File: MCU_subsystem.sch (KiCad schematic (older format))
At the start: 14 parts

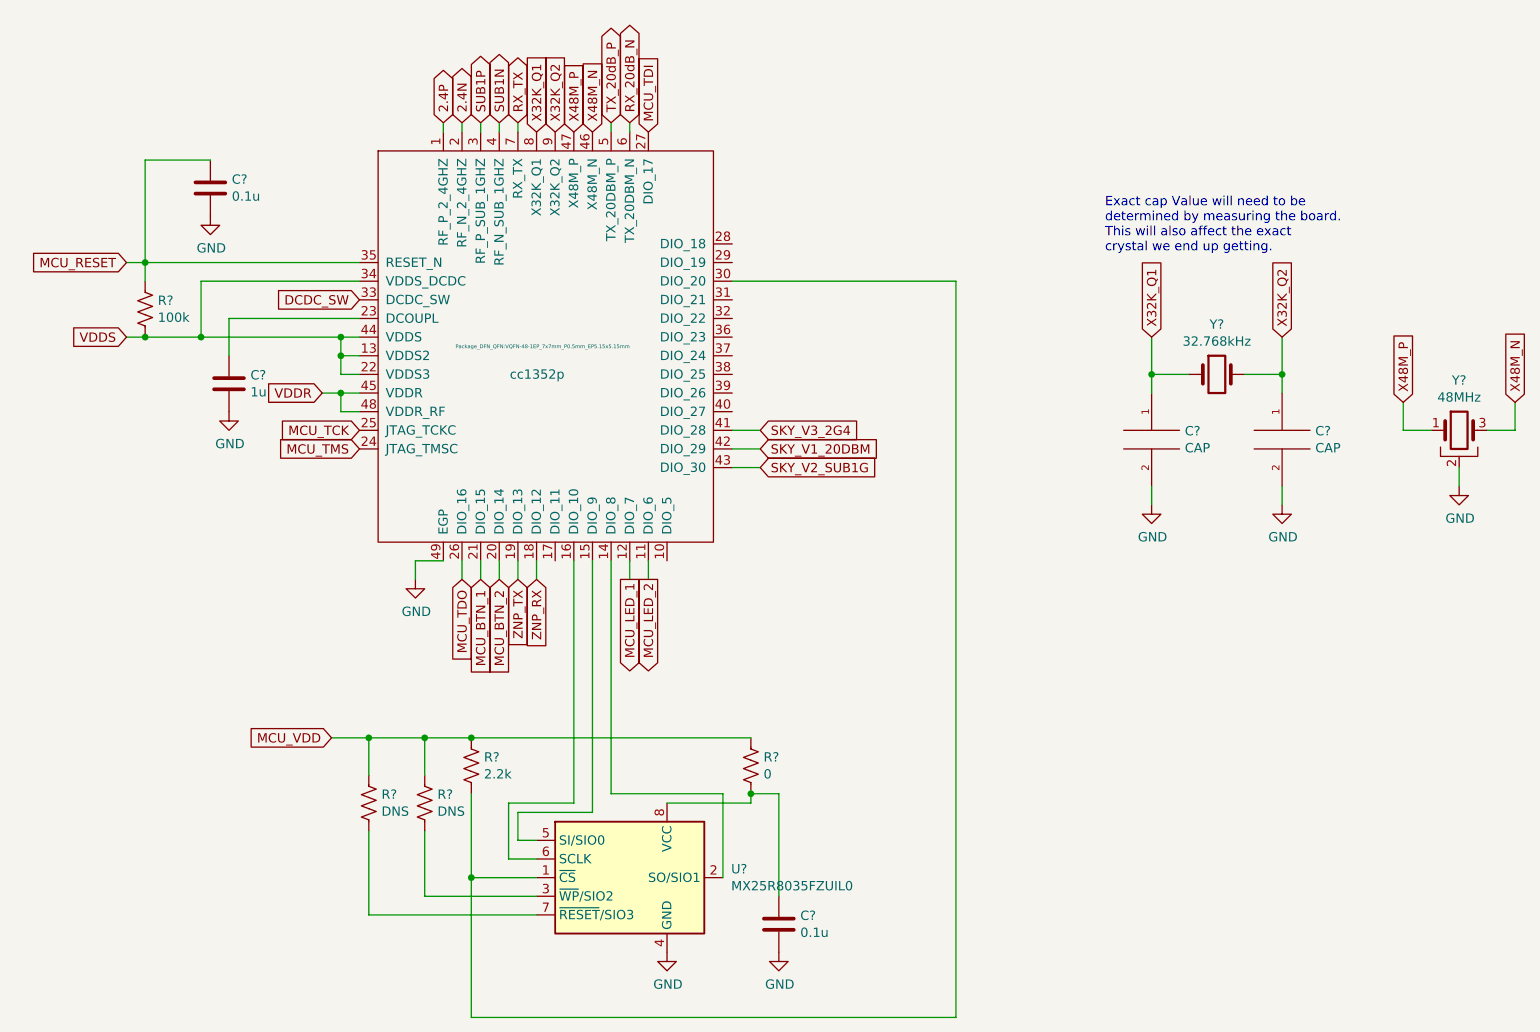
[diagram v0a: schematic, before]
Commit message: Revert "Added Flash IC and PB/LED footprints."
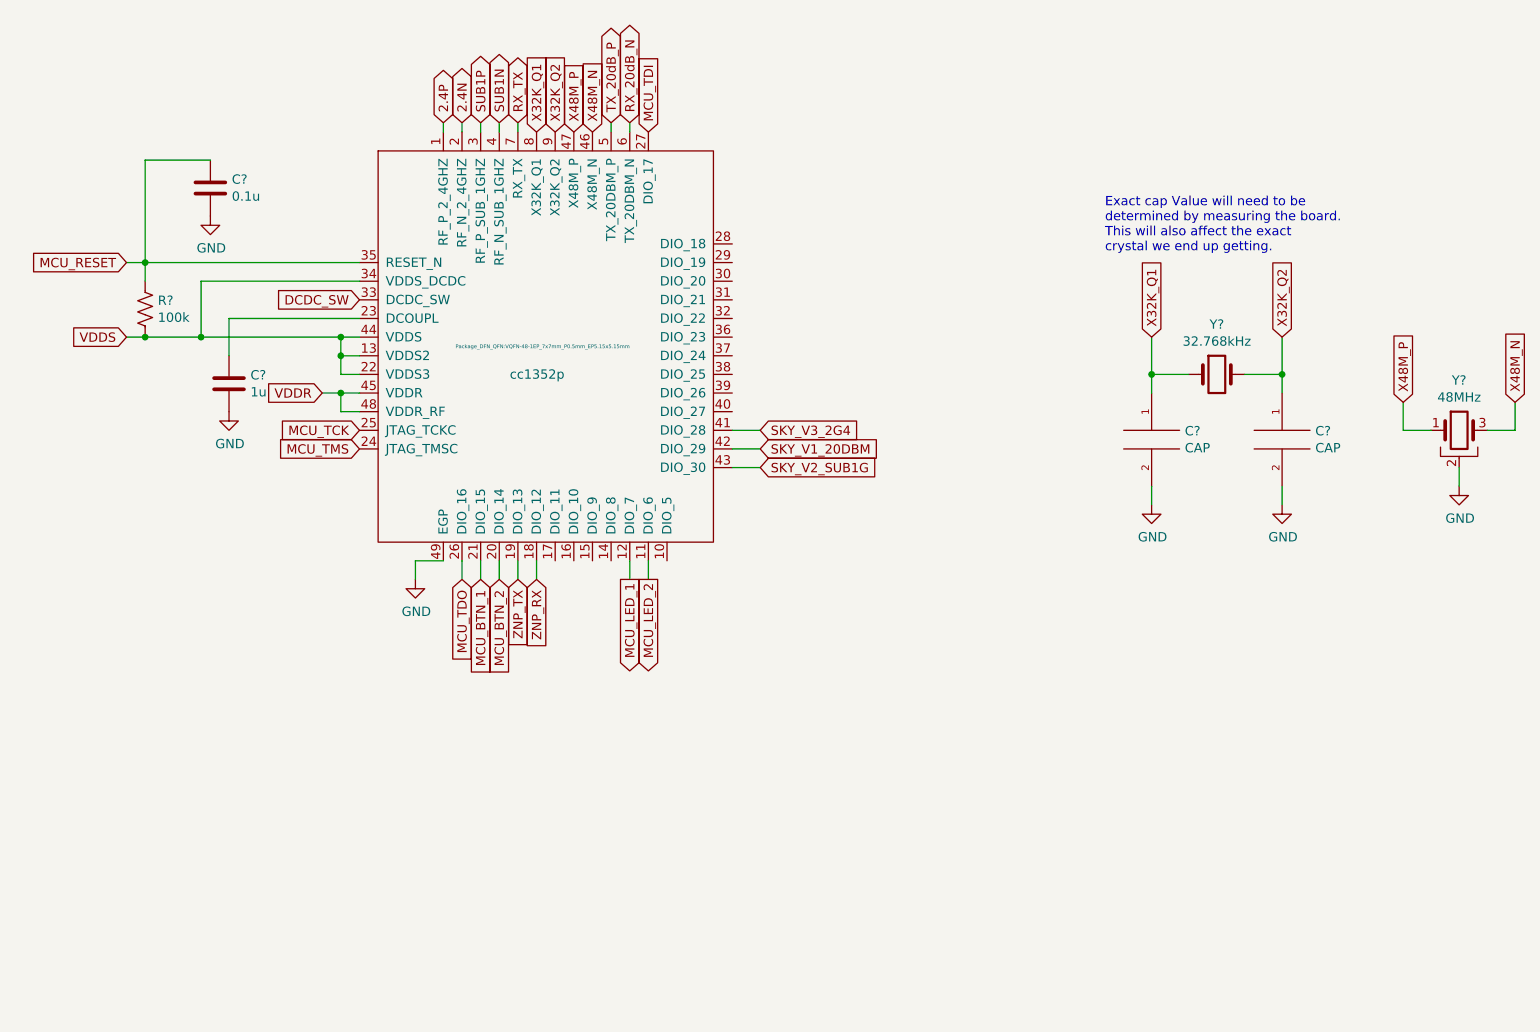
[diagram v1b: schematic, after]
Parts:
- removed C?: 0.1u, Capacitor_SMD:C_0805_2012Metric_Pad1.18x1.45mm_HandSolder, symbol Device:C
- removed R?: 2.2k, Resistor_SMD:R_0805_2012Metric_Pad1.20x1.40mm_HandSolder, symbol Device:R_US
- removed R?: 0, Resistor_SMD:R_0805_2012Metric_Pad1.20x1.40mm_HandSolder, symbol Device:R_US
- removed R? (x2): DNS, Resistor_SMD:R_0805_2012Metric_Pad1.20x1.40mm_HandSolder, symbol Device:R_US
- removed U?: MX25R8035FZUIL0, Package_SO:SOP-8_5.28x5.23mm_P1.27mm, symbol FLASH:MX25R8035FZUIL0
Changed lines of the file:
@@
 Text Notes 6850 3350 0    50   ~ 0
 Exact cap Value will need to be \ndetermined by measuring the board. \nThis will also affect the exact \ncrystal we end up getting.
-$Comp
-L power:GND #PWR?
-U 1 1 614D787A
-P 4500 7100
-F 0 "#PWR?" H 4500 6850 50  0001 C CNN
-F 1 "GND" H 4505 6927 50  0000 C CNN
-F 2 "" H 4500 7100 50  0001 C CNN
-F 3 "" H 4500 7100 50  0001 C CNN
-	1    4500 7100
-	1    0    0    -1
-$EndComp
-$Comp
-L power:GND #PWR?
-U 1 1 614D8142
-P 5100 7100
-F 0 "#PWR?" H 5100 6850 50  0001 C CNN
-F 1 "GND" H 5105 6927 50  0000 C CNN
-F 2 "" H 5100 7100 50  0001 C CNN
-F 3 "" H 5100 7100 50  0001 C CNN
-	1    5100 7100
-	1    0    0    -1
-$EndComp
-Text GLabel 2700 5950 0    50   Input ~ 0
-MCU_VDD
-$Comp
-L Device:R_US R?
-U 1 1 614D91BC
-P 3450 6100
-F 0 "R?" H 3518 6146 50  0000 L CNN
-F 1 "2.2k" H 3518 6055 50  0000 L CNN
-F 2 "Resistor_SMD:R_0805_2012Metric_Pad1.20x1.40mm_HandSolder" V 3490 6090 50  0001 C CNN
-F 3 "~" H 3450 6100 50  0001 C CNN
-	1    3450 6100
-	1    0    0    -1
-$EndComp
-Wire Wire Line
-	3800 6700 3450 6700
-Wire Wire Line
-	3450 6700 3450 6250
-Wire Wire Line
-	3200 5950 3450 5950
-$Comp
-L Device:R_US R?
-U 1 1 614DDC0C
-P 4950 6100
-F 0 "R?" H 5018 6146 50  0000 L CNN
-F 1 "0" H 5018 6055 50  0000 L CNN
-F 2 "Resistor_SMD:R_0805_2012Metric_Pad1.20x1.40mm_HandSolder" V 4990 6090 50  0001 C CNN
-F 3 "~" H 4950 6100 50  0001 C CNN
-	1    4950 6100
-	1    0    0    -1
-$EndComp
-$Comp
-L Device:C C?
-U 1 1 614E11ED
-P 5100 6950
-F 0 "C?" H 5215 6996 50  0000 L CNN
-F 1 "0.1u" H 5215 6905 50  0000 L CNN
-F 2 "Capacitor_SMD:C_0805_2012Metric_Pad1.18x1.45mm_HandSolder" H 5138 6800 50  0001 C CNN
-F 3 "~" H 5100 6950 50  0001 C CNN
-	1    5100 6950
-	1    0    0    -1
-$EndComp
-Wire Wire Line
-	5100 6800 5100 6250
-Wire Wire Line
-	5100 6250 4950 6250
-Wire Wire Line
-	4500 6300 4950 6300
-Wire Wire Line
-	4950 6300 4950 6250
-Connection ~ 4950 6250
-Wire Wire Line
-	4950 5950 3450 5950
-Connection ~ 3450 5950
-Wire Wire Line
-	3800 6600 3650 6600
-Wire Wire Line
-	3650 6600 3650 6300
-Wire Wire Line
-	3650 6300 4000 6300
-Wire Wire Line
-	4000 6300 4000 5000
-Wire Wire Line
-	4800 6250 4800 6700
-Wire Wire Line
-	3450 6700 3450 7450
-Wire Wire Line
-	3450 7450 6050 7450
-Wire Wire Line
-	6050 7450 6050 3500
-Wire Wire Line
-	6050 3500 4850 3500
-Connection ~ 3450 6700
-Wire Wire Line
-	4800 6250 4200 6250
-Wire Wire Line
-	4200 6250 4200 5000
-Wire Wire Line
-	4100 5000 4100 6350
-Wire Wire Line
-	4100 6350 3700 6350
-Wire Wire Line
-	3700 6350 3700 6500
-Wire Wire Line
-	3700 6500 3800 6500
-$Comp
-L Device:R_US R?
-U 1 1 614EF3D8
-P 2900 6300
-F 0 "R?" H 2968 6346 50  0000 L CNN
-F 1 "DNS" H 2968 6255 50  0000 L CNN
-F 2 "Resistor_SMD:R_0805_2012Metric_Pad1.20x1.40mm_HandSolder" V 2940 6290 50  0001 C CNN
-F 3 "~" H 2900 6300 50  0001 C CNN
-	1    2900 6300
-	1    0    0    -1
-$EndComp
-$Comp
-L Device:R_US R?
-U 1 1 614F0C42
-P 3200 6300
-F 0 "R?" H 3268 6346 50  0000 L CNN
-F 1 "DNS" H 3268 6255 50  0000 L CNN
-F 2 "Resistor_SMD:R_0805_2012Metric_Pad1.20x1.40mm_HandSolder" V 3240 6290 50  0001 C CNN
-F 3 "~" H 3200 6300 50  0001 C CNN
-	1    3200 6300
-	1    0    0    -1
-$EndComp
-Wire Wire Line
-	3800 6900 2900 6900
-Wire Wire Line
-	2900 6900 2900 6450
-Wire Wire Line
-	3200 6450 3200 6800
-Wire Wire Line
-	3200 6800 3800 6800
-Wire Wire Line
-	3200 6150 3200 5950
-Wire Wire Line
-	3200 5950 2900 5950
-Connection ~ 3200 5950
-Wire Wire Line
-	2900 6150 2900 5950
-Connection ~ 2900 5950
-Wire Wire Line
-	2900 5950 2700 5950
-$Comp
-L FLASH:MX25R8035FZUIL0 U?
-U 1 1 615019E6
-P 4300 6700
-F 0 "U?" H 4844 6746 50  0000 L CNN
-F 1 "MX25R8035FZUIL0" H 4844 6655 50  0000 L CNN
-F 2 "Package_SO:SOP-8_5.28x5.23mm_P1.27mm" H 4300 6100 50  0001 C CNN
-F 3 "http://www.macronix.com/Lists/Datasheet/Attachments/7534/MX25R3235F,%20Wide%20Range,%2032Mb,%20v1.6.pdf" H 4300 6700 50  0001 C CNN
-	1    4300 6700
-	1    0    0    -1
-$EndComp
 $EndSCHEMATC

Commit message: Added Flash IC and PB/LED footprints.
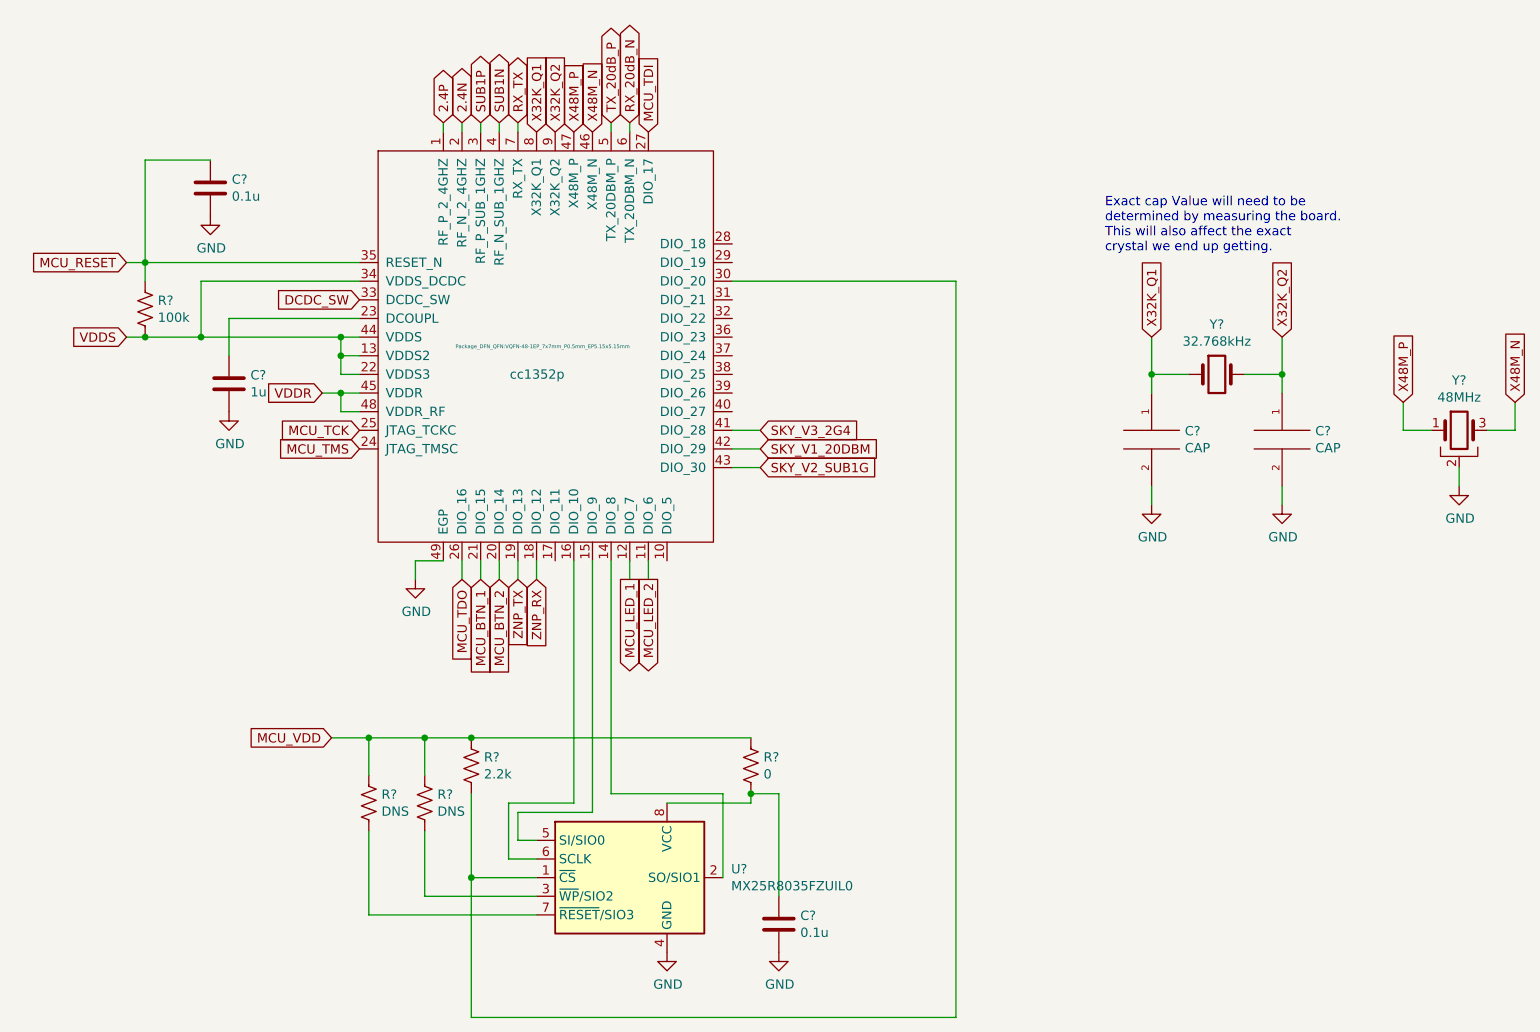
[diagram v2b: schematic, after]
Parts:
- added C?: 0.1u, Capacitor_SMD:C_0805_2012Metric_Pad1.18x1.45mm_HandSolder, symbol Device:C
- added R?: 2.2k, Resistor_SMD:R_0805_2012Metric_Pad1.20x1.40mm_HandSolder, symbol Device:R_US
- added R?: 0, Resistor_SMD:R_0805_2012Metric_Pad1.20x1.40mm_HandSolder, symbol Device:R_US
- added R? (x2): DNS, Resistor_SMD:R_0805_2012Metric_Pad1.20x1.40mm_HandSolder, symbol Device:R_US
- added U?: MX25R8035FZUIL0, Package_SO:SOP-8_5.28x5.23mm_P1.27mm, symbol FLASH:MX25R8035FZUIL0
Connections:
- net GND: now also C?.2, U?.4 (GND)
- net at U?.14 (DIO_8): now also U?.2 (SO/SIO1)
- net at U?.15 (DIO_9): now also U?.5 (SI/SIO0)
- net at U?.16 (DIO_10): now also U?.6 (SCLK)
- net at U?.30 (DIO_20): now also R?.2, U?.1 (~CS)
- new net: C?.1, R?.2, U?.8 (VCC)
- new net: R?.2, U?.7 (~RESET~/SIO3)
- new net: R?.2, U?.3 (~WP~/SIO2)
- new net MCU_VDD: R?.1, R?.1, R?.1, R?.1
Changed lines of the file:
@@
 Text Notes 6850 3350 0    50   ~ 0
 Exact cap Value will need to be \ndetermined by measuring the board. \nThis will also affect the exact \ncrystal we end up getting.
+$Comp
+L power:GND #PWR?
+U 1 1 614D787A
+P 4500 7100
+F 0 "#PWR?" H 4500 6850 50  0001 C CNN
+F 1 "GND" H 4505 6927 50  0000 C CNN
+F 2 "" H 4500 7100 50  0001 C CNN
+F 3 "" H 4500 7100 50  0001 C CNN
+	1    4500 7100
+	1    0    0    -1
+$EndComp
+$Comp
+L power:GND #PWR?
+U 1 1 614D8142
+P 5100 7100
+F 0 "#PWR?" H 5100 6850 50  0001 C CNN
+F 1 "GND" H 5105 6927 50  0000 C CNN
+F 2 "" H 5100 7100 50  0001 C CNN
+F 3 "" H 5100 7100 50  0001 C CNN
+	1    5100 7100
+	1    0    0    -1
+$EndComp
+Text GLabel 2700 5950 0    50   Input ~ 0
+MCU_VDD
+$Comp
+L Device:R_US R?
+U 1 1 614D91BC
+P 3450 6100
+F 0 "R?" H 3518 6146 50  0000 L CNN
+F 1 "2.2k" H 3518 6055 50  0000 L CNN
+F 2 "Resistor_SMD:R_0805_2012Metric_Pad1.20x1.40mm_HandSolder" V 3490 6090 50  0001 C CNN
+F 3 "~" H 3450 6100 50  0001 C CNN
+	1    3450 6100
+	1    0    0    -1
+$EndComp
+Wire Wire Line
+	3800 6700 3450 6700
+Wire Wire Line
+	3450 6700 3450 6250
+Wire Wire Line
+	3200 5950 3450 5950
+$Comp
+L Device:R_US R?
+U 1 1 614DDC0C
+P 4950 6100
+F 0 "R?" H 5018 6146 50  0000 L CNN
+F 1 "0" H 5018 6055 50  0000 L CNN
+F 2 "Resistor_SMD:R_0805_2012Metric_Pad1.20x1.40mm_HandSolder" V 4990 6090 50  0001 C CNN
+F 3 "~" H 4950 6100 50  0001 C CNN
+	1    4950 6100
+	1    0    0    -1
+$EndComp
+$Comp
+L Device:C C?
+U 1 1 614E11ED
+P 5100 6950
+F 0 "C?" H 5215 6996 50  0000 L CNN
+F 1 "0.1u" H 5215 6905 50  0000 L CNN
+F 2 "Capacitor_SMD:C_0805_2012Metric_Pad1.18x1.45mm_HandSolder" H 5138 6800 50  0001 C CNN
+F 3 "~" H 5100 6950 50  0001 C CNN
+	1    5100 6950
+	1    0    0    -1
+$EndComp
+Wire Wire Line
+	5100 6800 5100 6250
+Wire Wire Line
+	5100 6250 4950 6250
+Wire Wire Line
+	4500 6300 4950 6300
+Wire Wire Line
+	4950 6300 4950 6250
+Connection ~ 4950 6250
+Wire Wire Line
+	4950 5950 3450 5950
+Connection ~ 3450 5950
+Wire Wire Line
+	3800 6600 3650 6600
+Wire Wire Line
+	3650 6600 3650 6300
+Wire Wire Line
+	3650 6300 4000 6300
+Wire Wire Line
+	4000 6300 4000 5000
+Wire Wire Line
+	4800 6250 4800 6700
+Wire Wire Line
+	3450 6700 3450 7450
+Wire Wire Line
+	3450 7450 6050 7450
+Wire Wire Line
+	6050 7450 6050 3500
+Wire Wire Line
+	6050 3500 4850 3500
+Connection ~ 3450 6700
+Wire Wire Line
+	4800 6250 4200 6250
+Wire Wire Line
+	4200 6250 4200 5000
+Wire Wire Line
+	4100 5000 4100 6350
+Wire Wire Line
+	4100 6350 3700 6350
+Wire Wire Line
+	3700 6350 3700 6500
+Wire Wire Line
+	3700 6500 3800 6500
+$Comp
+L Device:R_US R?
+U 1 1 614EF3D8
+P 2900 6300
+F 0 "R?" H 2968 6346 50  0000 L CNN
+F 1 "DNS" H 2968 6255 50  0000 L CNN
+F 2 "Resistor_SMD:R_0805_2012Metric_Pad1.20x1.40mm_HandSolder" V 2940 6290 50  0001 C CNN
+F 3 "~" H 2900 6300 50  0001 C CNN
+	1    2900 6300
+	1    0    0    -1
+$EndComp
+$Comp
+L Device:R_US R?
+U 1 1 614F0C42
+P 3200 6300
+F 0 "R?" H 3268 6346 50  0000 L CNN
+F 1 "DNS" H 3268 6255 50  0000 L CNN
+F 2 "Resistor_SMD:R_0805_2012Metric_Pad1.20x1.40mm_HandSolder" V 3240 6290 50  0001 C CNN
+F 3 "~" H 3200 6300 50  0001 C CNN
+	1    3200 6300
+	1    0    0    -1
+$EndComp
+Wire Wire Line
+	3800 6900 2900 6900
+Wire Wire Line
+	2900 6900 2900 6450
+Wire Wire Line
+	3200 6450 3200 6800
+Wire Wire Line
+	3200 6800 3800 6800
+Wire Wire Line
+	3200 6150 3200 5950
+Wire Wire Line
+	3200 5950 2900 5950
+Connection ~ 3200 5950
+Wire Wire Line
+	2900 6150 2900 5950
+Connection ~ 2900 5950
+Wire Wire Line
+	2900 5950 2700 5950
+$Comp
+L FLASH:MX25R8035FZUIL0 U?
+U 1 1 615019E6
+P 4300 6700
+F 0 "U?" H 4844 6746 50  0000 L CNN
+F 1 "MX25R8035FZUIL0" H 4844 6655 50  0000 L CNN
+F 2 "Package_SO:SOP-8_5.28x5.23mm_P1.27mm" H 4300 6100 50  0001 C CNN
+F 3 "http://www.macronix.com/Lists/Datasheet/Attachments/7534/MX25R3235F,%20Wide%20Range,%2032Mb,%20v1.6.pdf" H 4300 6700 50  0001 C CNN
+	1    4300 6700
+	1    0    0    -1
+$EndComp
 $EndSCHEMATC
